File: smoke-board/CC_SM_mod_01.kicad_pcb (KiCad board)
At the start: 2 copper layers, 36.8 x 58.4 mm, 26 parts, among them P1 CONN_01X03, Q1 BC847, U1 A5366

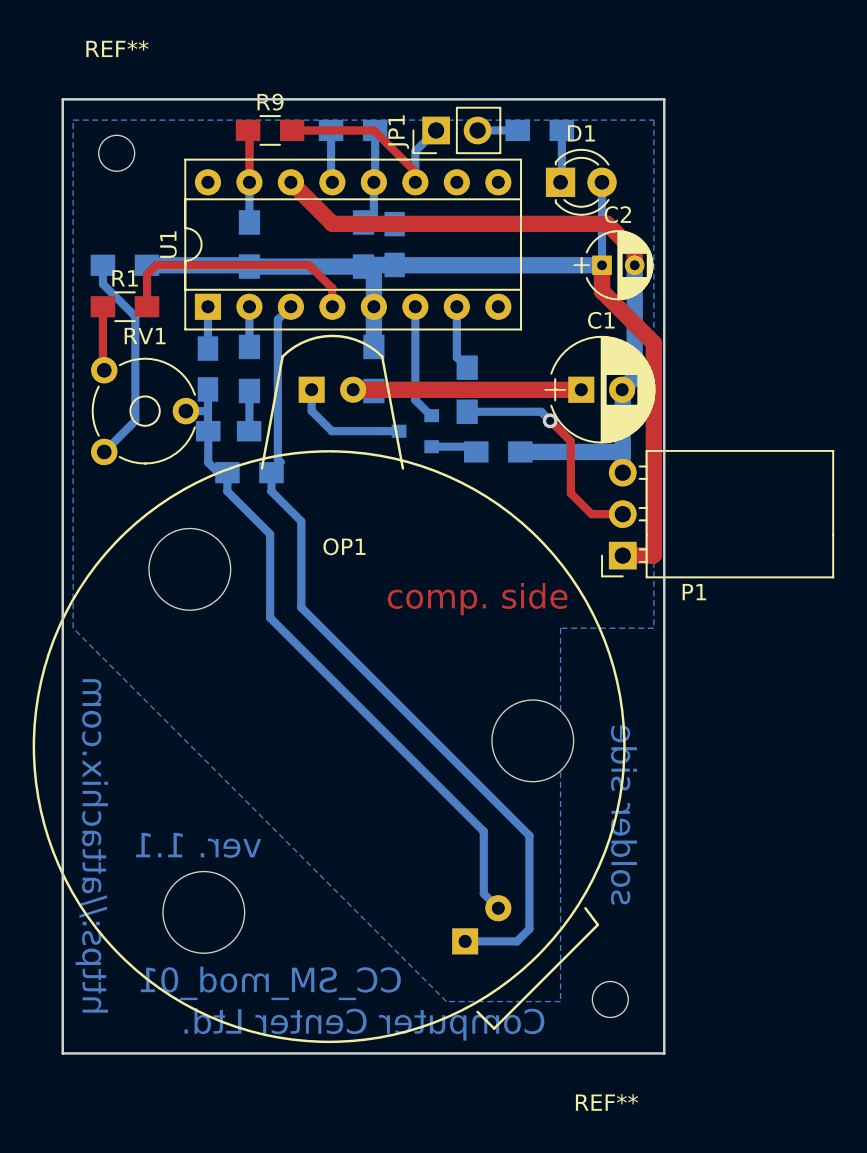
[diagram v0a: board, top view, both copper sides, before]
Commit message: Slightly moved the holes so that the smoke PCB does not push the walls of the enclosure.
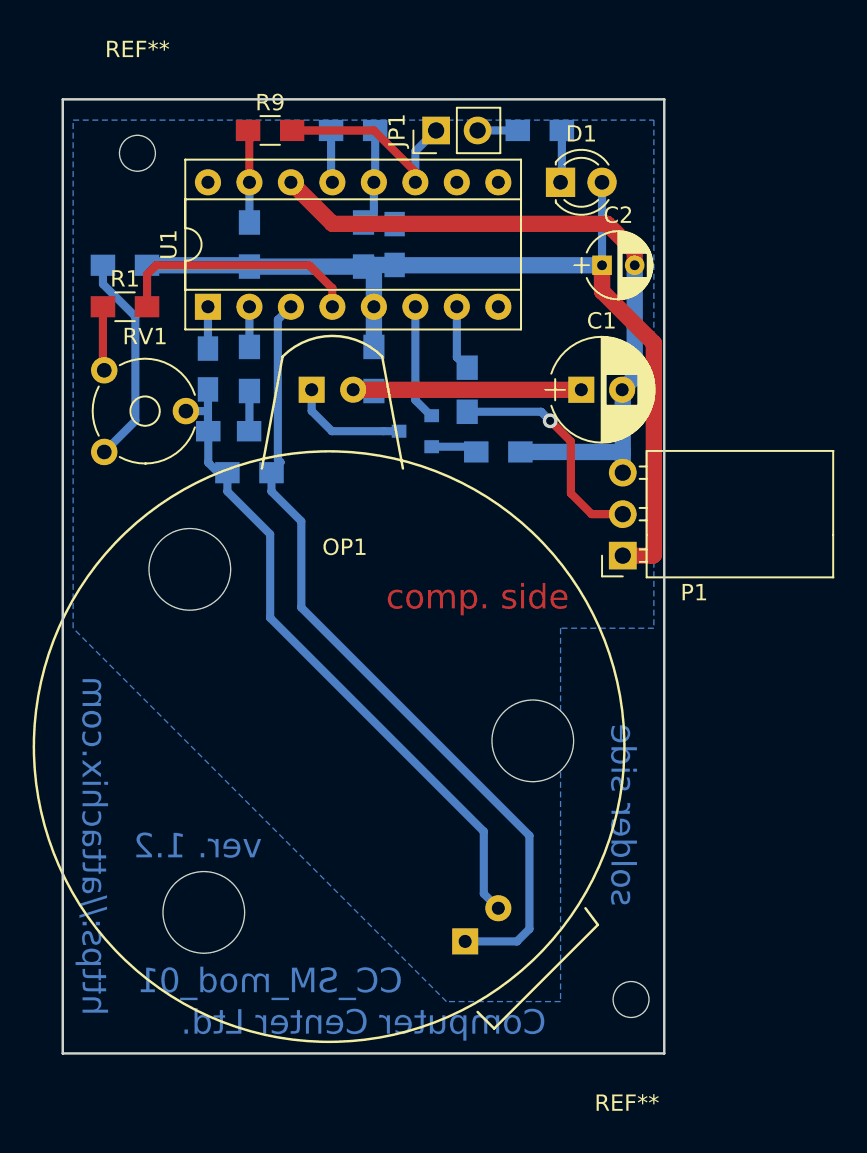
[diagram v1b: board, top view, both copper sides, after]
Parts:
- moved REF** 1.27 mm to (121.4, 92.2)
- moved REF** 1.27 mm to (151.6, 144.0)
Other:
- board text added: "ver. 1.2"
- board text removed: "ver. 1.1"
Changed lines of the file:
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@@
     (links 41)
     (no_connects 0)
-    (area 116.764999 88.824999 153.745001 147.395001)
+    (area 105.180001 84.827 164.499001 154.465)
     (thickness 1.6)
     (drawings 20)
@@
     (mod_text_size 1 1)
     (mod_text_width 0.15)
-    (pad_size 1.524 1.524)
-    (pad_drill 0.762)
+    (pad_size 2.2 2.2)
+    (pad_drill 2.2)
     (pad_to_mask_clearance 0.2)
     (aux_axis_origin 0 0)
@@
     (pad 16 thru_hole oval (at 7.62 0 90) (size 1.6 1.6) (drill 0.8) (layers *.Cu *.Mask)
       (net 26 "Net-(U1-Pad16)"))
-    (model Housings_DIP.3dshapes/DIP-16_W7.62mm_Socket.wrl
-      (at (xyz 0 0 0))
-      (scale (xyz 1 1 1))
-      (rotate (xyz 0 0 0))
-    )
     (model Package_DIP.3dshapes/DIP-16_W7.62mm.wrl
       (at (xyz 0 0 0))
@@
   )
   (module Mounting_Holes:MountingHole_2.2mm_M2 (layer F.Cu)
-    (at 120.142 92.202)
+    (at 121.412 92.202)
     (descr "Mounting Hole 2.2mm, no annular, M2")
     (tags "mounting hole 2.2mm no annular m2")
@@
   )
   (module Mounting_Holes:MountingHole_2.2mm_M2 (layer F.Cu)
-    (at 150.368 144.018)
+    (at 151.638 144.018)
     (descr "Mounting Hole 2.2mm, no annular, M2")
     (tags "mounting hole 2.2mm no annular m2")
@@
     (pad 1 np_thru_hole circle (at 0 0) (size 2.2 2.2) (drill 2.2) (layers *.Cu *.Mask))
   )
-  (gr_text "ver. 1.1" (at 125.095 134.62) (layer B.Cu)
+  (gr_text "ver. 1.2" (at 125.095 134.62) (layer B.Cu)
     (effects (font (size 1.5 1.5) (thickness 0.3)) (justify mirror))
   )
@@
   (segment (start 139.43 110.17) (end 141.84 110.17) (width 0.5) (layer B.Cu) (net 2))
   (segment (start 141.84 110.17) (end 142.16 110.49) (width 0.5) (layer B.Cu) (net 2))
-  (segment (start 132.08 106.68) (end 132.08 107.98) (width 0.5) (layer B.Cu) (net 3))
+  (segment (start 132.08 106.68) (end 132.08 107.98) (width 0.5) (layer B.Cu) (net 3) (status 10))
   (segment (start 132.08 107.98) (end 133.32 109.22) (width 0.5) (layer B.Cu) (net 3))
   (segment (start 133.32 109.22) (end 136.48 109.22) (width 0.5) (layer B.Cu) (net 3))
   (segment (start 136.48 109.22) (end 137.43 109.22) (width 0.5) (layer B.Cu) (net 3))
-  (segment (start 148.59 106.68) (end 134.62 106.68) (width 1) (layer F.Cu) (net 4))
-  (segment (start 134.62 106.68) (end 135.81 106.68) (width 1) (layer B.Cu) (net 4))
+  (segment (start 148.59 106.68) (end 134.62 106.68) (width 1) (layer F.Cu) (net 4) (status 20))
+  (segment (start 134.62 106.68) (end 135.81 106.68) (width 1) (layer B.Cu) (net 4) (status 10))
   (segment (start 135.81 106.68) (end 135.89 106.76) (width 1) (layer B.Cu) (net 4))
   (segment (start 133.35 96.52) (end 150.168528 96.52) (width 1) (layer F.Cu) (net 5))
@@
   (segment (start 126.92 112.91) (end 126.92 111.76) (width 0.5) (layer B.Cu) (net 8))
   (segment (start 142.619999 133.729999) (end 129.54 120.65) (width 0.5) (layer B.Cu) (net 8))
-  (segment (start 143.51 138.43) (end 142.619999 137.539999) (width 0.5) (layer B.Cu) (net 8))
+  (segment (start 143.51 138.43) (end 142.619999 137.539999) (width 0.5) (layer B.Cu) (net 8) (status 10))
   (segment (start 142.619999 137.539999) (end 142.619999 133.729999) (width 0.5) (layer B.Cu) (net 8))
   (segment (start 126.365 111.76) (end 125.75 111.145) (width 0.5) (layer B.Cu) (net 8))
@@
   (segment (start 129.62 111.68) (end 130.175 111.125) (width 0.5) (layer B.Cu) (net 14))
   (segment (start 129.62 111.76) (end 129.62 111.68) (width 0.5) (layer B.Cu) (net 14))
-  (segment (start 141.478 140.462) (end 144.653 140.462) (width 0.5) (layer B.Cu) (net 14))
+  (segment (start 141.478 140.462) (end 144.653 140.462) (width 0.5) (layer B.Cu) (net 14) (status 10))
   (segment (start 144.653 140.462) (end 145.415 139.7) (width 0.5) (layer B.Cu) (net 14))
   (segment (start 145.415 139.7) (end 145.415 133.985) (width 0.5) (layer B.Cu) (net 14))
